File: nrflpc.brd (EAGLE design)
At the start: 67.9 x 38.8 mm, 71 parts, among them IC1 LPC1111/12/13/14-HVQFN33, IC2 LT1763CS8-3.3, IC3 LM3401, IC5 LM3401, IC6 LM3401, IC7 LM3401, IC8 78L05SMD, Q1 20MHz, Q2 MOSFET-PCHANNEL, Q3 MOSFET-PCHANNEL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

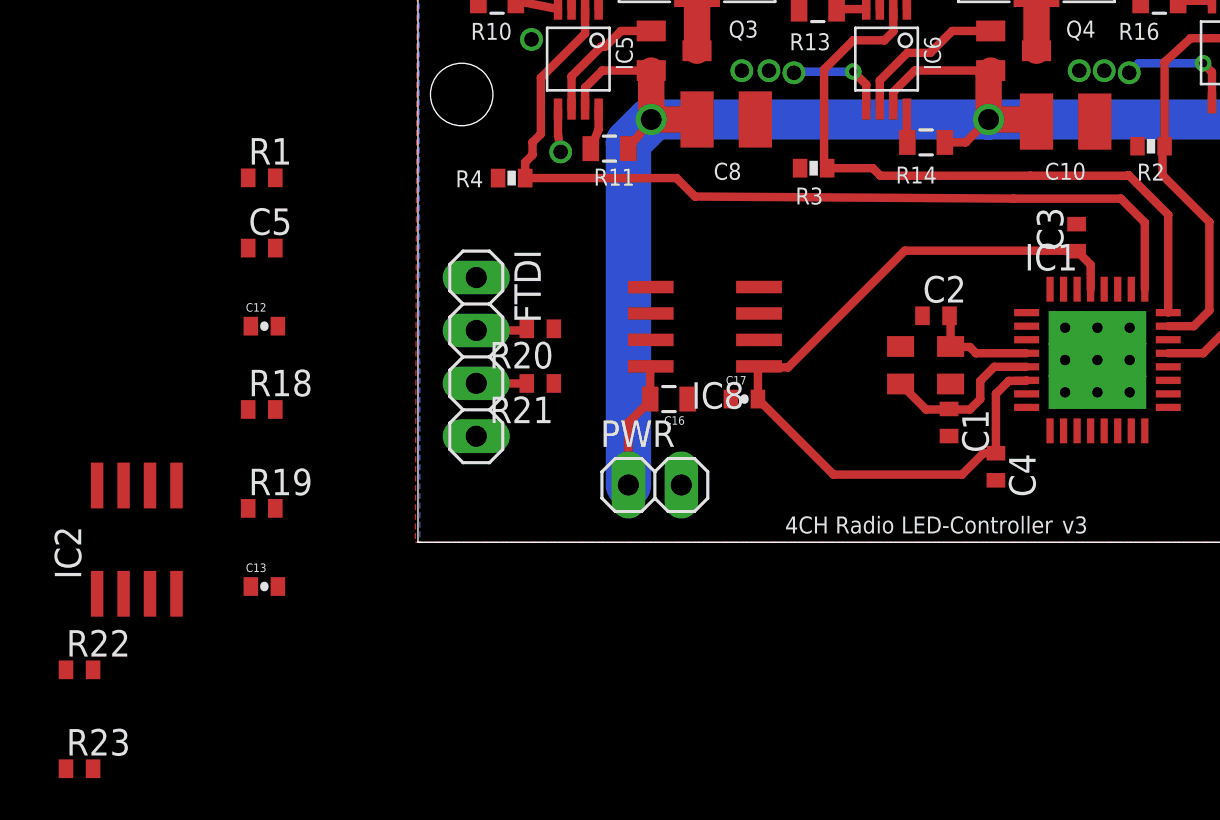
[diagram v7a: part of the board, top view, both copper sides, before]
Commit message: Removed unnecessary pullups, new 3.3V regulator, begin routing
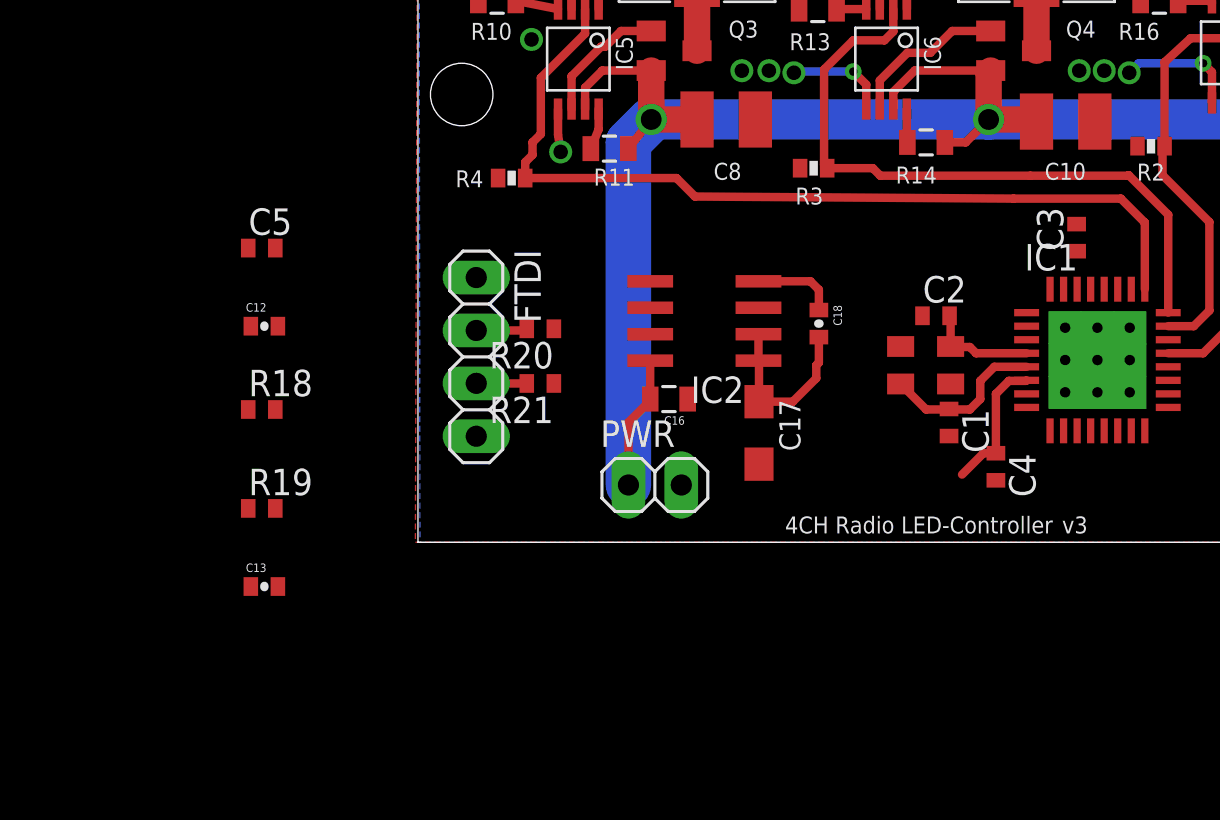
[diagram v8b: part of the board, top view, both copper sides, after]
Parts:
- removed IC8: 78L05SMD, linear:SO08
- removed R1, R23: 15k, rcl:R0402
- removed R22: 150, rcl:R0402
- added C18: 10nF, SparkFun:0402-CAP
- C17: value 100nF -> 10µF; device SparkFun:0402-CAP -> rcl:SMC_A
- moved IC2 29.2 mm to (13.8, 10.6), turned to 90 degrees
- moved C17 1.77 mm to (16.4, 5.25), turned to 270 degrees
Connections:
- net !RST: no longer R1.1
- net +12V: now also IC2.8; no longer IC8.8
- net +3V3: now also C17.+, C18.2, IC2.1, IC2.2; no longer C17.2, IC8.1, R1.2, R23.2
- net BOOTL: now also IC1.3; no longer R22.2
- net GND: now also C17.-; no longer C17.1, IC8.2, IC8.3, IC8.6, IC8.7
- net N$18: now also C18.1, IC2.4; no longer IC1.3, R22.1, R23.1
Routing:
- net +3V3: track 39.3 -> 15.1 mm
- net N$18: track 0.00 -> 4.04 mm
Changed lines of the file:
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@@
 <attribute name="VALUE" x="41.484" y="34.503" size="0.4064" layer="27"/>
 </element>
-<element name="IC8" library="linear" package="SO08" value="78L05SMD" x="13.775" y="10.35" rot="R90"/>
 <element name="C16" library="SparkFun" package="0805" value="1µF" x="12.05" y="6.875" rot="R180"/>
-<element name="C17" library="SparkFun" package="0402-CAP" value="100nF" x="15.675" y="6.875"/>
 <element name="FTDI" library="pinhead" package="1X04" value="" x="2.8" y="8.9" rot="R270"/>
 <element name="JP1" library="pinhead" package="2X04" value="" x="54.75" y="8.55" rot="R90"/>
@@
 <element name="C3" library="rcl" package="C0402" value="100nF" x="31.625" y="14.625" rot="R90"/>
 <element name="C4" library="rcl" package="C0402" value="100nF" x="27.75" y="3.625" rot="R270"/>
-<element name="R1" library="rcl" package="R0402" value="15k" x="-7.5" y="17.5"/>
 <element name="C5" library="rcl" package="C0402" value="100nF" x="-7.5" y="14.125"/>
 <element name="PWR" library="pinhead" package="1X02" value="" x="11.375" y="2.75"/>
@@
 <element name="R20" library="rcl" package="R0402" value="150" x="5.875" y="10.25" rot="R180"/>
 <element name="R21" library="rcl" package="R0402" value="150" x="5.875" y="7.625" rot="R180"/>
-<element name="IC2" library="linear-technology" package="SOIC8" value="LT1763CS8-3.3" x="-13.5" y="0.125">
-<attribute name="OC_NEWARK" value="57M6055" x="-13.5" y="0.125" size="1.778" layer="27" display="off"/>
-<attribute name="MPN" value="LT1763CS8-3.3" x="-13.5" y="0.125" size="1.778" layer="27" display="off"/>
-<attribute name="MF" value="" x="-13.5" y="0.125" size="1.778" layer="27" display="off"/>
-<attribute name="OC_FARNELL" value="1273617" x="-13.5" y="0.125" size="1.778" layer="27" display="off"/>
+<element name="IC2" library="linear-technology" package="SOIC8" value="LT1763CS8-3.3" x="13.75" y="10.625" rot="R90">
+<attribute name="OC_NEWARK" value="57M6055" x="13.75" y="10.625" size="1.778" layer="27" rot="R90" display="off"/>
+<attribute name="MPN" value="LT1763CS8-3.3" x="13.75" y="10.625" size="1.778" layer="27" rot="R90" display="off"/>
+<attribute name="MF" value="" x="13.75" y="10.625" size="1.778" layer="27" rot="R90" display="off"/>
+<attribute name="OC_FARNELL" value="1273617" x="13.75" y="10.625" size="1.778" layer="27" rot="R90" display="off"/>
 </element>
-<element name="R22" library="rcl" package="R0402" value="150" x="-16.25" y="-6.125"/>
-<element name="R23" library="rcl" package="R0402" value="15k" x="-16.25" y="-10.875"/>
+<element name="C18" library="SparkFun" package="0402-CAP" value="10nF" x="19.25" y="10.5" rot="R270"/>
+<element name="C17" library="rcl" package="SMC_A" value="10µF" x="16.375" y="5.25" rot="R270"/>
 </elements>
 <signals>
 <signal name="!RST">
 <contactref element="FTDI" pad="1"/>
-<contactref element="R1" pad="1"/>
 <contactref element="C5" pad="1"/>
 <contactref element="IC1" pad="2"/>
 <wire x1="2.8" y1="12.71" x2="29.225" y2="10.375" width="0" layer="19" extent="1-1"/>
 <wire x1="-8.15" y1="14.125" x2="2.8" y2="12.71" width="0" layer="19" extent="1-1"/>
-<wire x1="-8.15" y1="17.5" x2="-8.15" y2="14.125" width="0" layer="19" extent="1-1"/>
 </signal>
 <signal name="RXD">
@@
 <wire x1="54.8" y1="20.3" x2="60.2" y2="20.3" width="2.1844" layer="16"/>
 <wire x1="60.2" y1="20.3" x2="61" y2="21.1" width="2.1844" layer="16"/>
-<contactref element="C16" pad="2"/>
-<contactref element="IC8" pad="8"/>
-<wire x1="11.15" y1="6.875" x2="11.15" y2="8.42" width="0.4064" layer="1"/>
-<wire x1="11.15" y1="8.42" x2="11.175" y2="8.445" width="0.4064" layer="1"/>
-<wire x1="11.15" y1="6.875" x2="11.15" y2="6.795" width="0.4064" layer="1"/>
 <wire x1="11.15" y1="6.795" x2="10.105" y2="5.75" width="0.4064" layer="1"/>
 <wire x1="10.105" y1="5.75" x2="10.105" y2="2.75" width="0.4064" layer="1"/>
+<contactref element="IC2" pad="8"/>
+<contactref element="C16" pad="2"/>
+<wire x1="11.15" y1="6.875" x2="11.15" y2="8.72" width="0.4064" layer="1"/>
+<wire x1="11.15" y1="6.795" x2="11.15" y2="6.875" width="0" layer="19" extent="1-1"/>
 </signal>
 <signal name="TXD">
@@
 <vertex x="67.882" y="38.781"/>
 </polygon>
-<contactref element="IC8" pad="2"/>
-<contactref element="IC8" pad="3"/>
-<contactref element="IC8" pad="6"/>
-<contactref element="IC8" pad="7"/>
-<contactref element="IC8" pad="7"/>
-<contactref element="IC8" pad="6"/>
-<contactref element="IC8" pad="3"/>
-<contactref element="IC8" pad="2"/>
-<contactref element="C17" pad="1"/>
 <contactref element="C16" pad="1"/>
 <contactref element="FTDI" pad="4"/>
@@
 <contactref element="IC2" pad="6"/>
 <contactref element="IC2" pad="7"/>
+<contactref element="IC2" pad="3"/>
+<contactref element="IC2" pad="6"/>
+<contactref element="IC2" pad="7"/>
+<contactref element="C17" pad="-"/>
 <wire x1="31.625" y1="15.275" x2="32.625" y2="8.75" width="0" layer="19" extent="1-1"/>
-<wire x1="25.5" y1="5.1" x2="27.75" y2="2.975" width="0" layer="19" extent="1-1"/>
 <wire x1="-6.85" y1="14.125" x2="3.849" y2="17.4865" width="0" layer="19" extent="1-1"/>
 <wire x1="-8.025" y1="10.375" x2="-6.85" y2="14.125" width="0" layer="19" extent="1-1"/>
-<wire x1="-12.865" y1="2.725" x2="-8.025" y2="10.375" width="0" layer="19" extent="1-1"/>
-<wire x1="-14.135" y1="2.725" x2="-12.865" y2="2.725" width="0" layer="19" extent="1-1"/>
-<wire x1="-12.865" y1="-2.475" x2="-12.865" y2="2.725" width="0" layer="19" extent="1-1"/>
-<wire x1="-8.025" y1="-2.125" x2="-12.865" y2="-2.475" width="0" layer="19" extent="1-1"/>
+<wire x1="-8.025" y1="-2.125" x2="-8.025" y2="10.375" width="0" layer="19" extent="1-1"/>
 </signal>
 <signal name="N$1">
@@
 </signal>
 <signal name="+3V3">
-<contactref element="IC8" pad="1"/>
-<contactref element="C17" pad="2"/>
 <contactref element="JP1" pad="2"/>
 <contactref element="IC1" pad="29"/>
@@
 <contactref element="C3" pad="1"/>
 <contactref element="C4" pad="1"/>
-<contactref element="R1" pad="2"/>
-<wire x1="16.325" y1="6.875" x2="16.325" y2="8.395" width="0.4064" layer="1"/>
-<wire x1="16.325" y1="8.395" x2="16.375" y2="8.445" width="0.4064" layer="1"/>
 <wire x1="27.75" y1="4.275" x2="27.75" y2="7.125" width="0.4064" layer="1"/>
 <wire x1="27.75" y1="7.125" x2="28.375" y2="7.75" width="0.4064" layer="1"/>
@@
 <wire x1="27.75" y1="4.275" x2="27.15" y2="4.275" width="0.4064" layer="1"/>
 <wire x1="27.15" y1="4.275" x2="26.125" y2="3.25" width="0.4064" layer="1"/>
-<wire x1="26.125" y1="3.25" x2="19.95" y2="3.25" width="0.4064" layer="1"/>
-<wire x1="19.95" y1="3.25" x2="16.325" y2="6.875" width="0.4064" layer="1"/>
-<wire x1="16.325" y1="8.395" x2="17.77" y2="8.395" width="0.4064" layer="1"/>
-<wire x1="17.77" y1="8.395" x2="23.375" y2="14" width="0.4064" layer="1"/>
-<wire x1="23.375" y1="14" x2="31.625" y2="14" width="0.4064" layer="1"/>
-<wire x1="31.625" y1="14" x2="32.3" y2="13.325" width="0.4064" layer="1"/>
-<wire x1="32.3" y1="12.15" x2="32.3" y2="13.325" width="0.4064" layer="1"/>
-<contactref element="R23" pad="2"/>
+<contactref element="IC2" pad="1"/>
+<contactref element="C18" pad="2"/>
+<contactref element="IC2" pad="2"/>
+<wire x1="16.35" y1="8.72" x2="16.35" y2="9.99" width="0.4064" layer="1"/>
+<contactref element="C17" pad="+"/>
+<wire x1="16.375" y1="6.75" x2="16.375" y2="8.695" width="0.4064" layer="1"/>
+<wire x1="16.375" y1="8.695" x2="16.35" y2="8.72" width="0.4064" layer="1"/>
+<wire x1="19.25" y1="9.85" x2="19.25" y2="8.625" width="0.4064" layer="1"/>
+<wire x1="19.25" y1="8.625" x2="19.125" y2="8.5" width="0.4064" layer="1"/>
+<wire x1="19.125" y1="8.5" x2="19.125" y2="7.875" width="0.4064" layer="1"/>
+<wire x1="19.125" y1="7.875" x2="18" y2="6.75" width="0.4064" layer="1"/>
+<wire x1="18" y1="6.75" x2="16.375" y2="6.75" width="0.4064" layer="1"/>
 <wire x1="32.3" y1="12.15" x2="53.48" y2="4.74" width="0" layer="19" extent="1-1"/>
-<wire x1="31.625" y1="13.975" x2="31.625" y2="14" width="0" layer="19" extent="1-1"/>
-<wire x1="-6.85" y1="17.5" x2="16.325" y2="8.395" width="0" layer="19" extent="1-1"/>
-<wire x1="-15.6" y1="-10.875" x2="-6.85" y2="17.5" width="0" layer="19" extent="1-1"/>
+<wire x1="31.625" y1="13.975" x2="32.3" y2="12.15" width="0" layer="19" extent="1-1"/>
+<wire x1="29.225" y1="7.775" x2="32.3" y2="12.15" width="0" layer="19" extent="1-1"/>
+<wire x1="19.125" y1="7.875" x2="26.125" y2="3.25" width="0" layer="19" extent="1-1"/>
 </signal>
 <signal name="CE">
@@
 <wire x1="6.525" y1="7.625" x2="30.35" y2="12.15" width="0" layer="19" extent="1-1"/>
 </signal>
+<signal name="BOOTL">
+<contactref element="IC1" pad="3"/>
+</signal>
 <signal name="N$18">
-<contactref element="IC1" pad="3"/>
-<contactref element="R22" pad="1"/>
-<contactref element="R23" pad="1"/>
-<wire x1="-16.9" y1="-6.125" x2="29.225" y2="9.725" width="0" layer="19" extent="1-1"/>
-<wire x1="-16.9" y1="-10.875" x2="-16.9" y2="-6.125" width="0" layer="19" extent="1-1"/>
-</signal>
-<signal name="BOOTL">
-<contactref element="R22" pad="2"/>
+<contactref element="IC2" pad="4"/>
+<contactref element="C18" pad="1"/>
+<wire x1="16.35" y1="12.53" x2="18.845" y2="12.53" width="0.4064" layer="1"/>
+<wire x1="18.845" y1="12.53" x2="19.25" y2="12.125" width="0.4064" layer="1"/>
+<wire x1="19.25" y1="12.125" x2="19.25" y2="11.15" width="0.4064" layer="1"/>
 </signal>
 </signals>
